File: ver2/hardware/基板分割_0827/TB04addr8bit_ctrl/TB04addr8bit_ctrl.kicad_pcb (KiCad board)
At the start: 2 copper layers, 210 x 170 mm, 101 parts, among them IC401 74HC161N, IC402 74HC161N, IC601 74HC161N, J1 Conn_02x20_Odd_Even, J1602 Screw_Terminal_01x02, J2 Conn_02x20_Odd_Even, J3 Conn_02x10_Odd_Even, J6 Conn_02x05_Odd_Even, J7 Conn_02x05_Odd_Even, J8 Conn_02x05_Odd_Even, J801 Conn_02x05_Odd_Even, J802 Conn_02x05_Odd_Even, J803 Conn_02x05_Odd_Even, J804 Conn_02x05_Odd_Even, J9 Conn_02x05_Odd_Even, SW601 SW_Coded_SH-7050, U101 74HC157, U1101 6116, U1102 74HC244, U1103 74HC244, U1201 74HC193, U1301 74HC08, U1401 74HC138, U1402 74HC244, U1403 74HC244, U1404 74HC244, U1405 74HC244, U1406 74HC157, U1407 74HC139, U1501 74AHC04, U1503 74HC08, U1504 74HC00, U1505 74HC00, U1506 74HC32, U1509 74HC10, U401 74HC157, U404 74HC157, U601 74HC273, U602 74HC273, U604 28C256, U606 74HC273, U607 74HC238, U701 74HC273, U703 28C256, U705 74HC273, U706 28C256

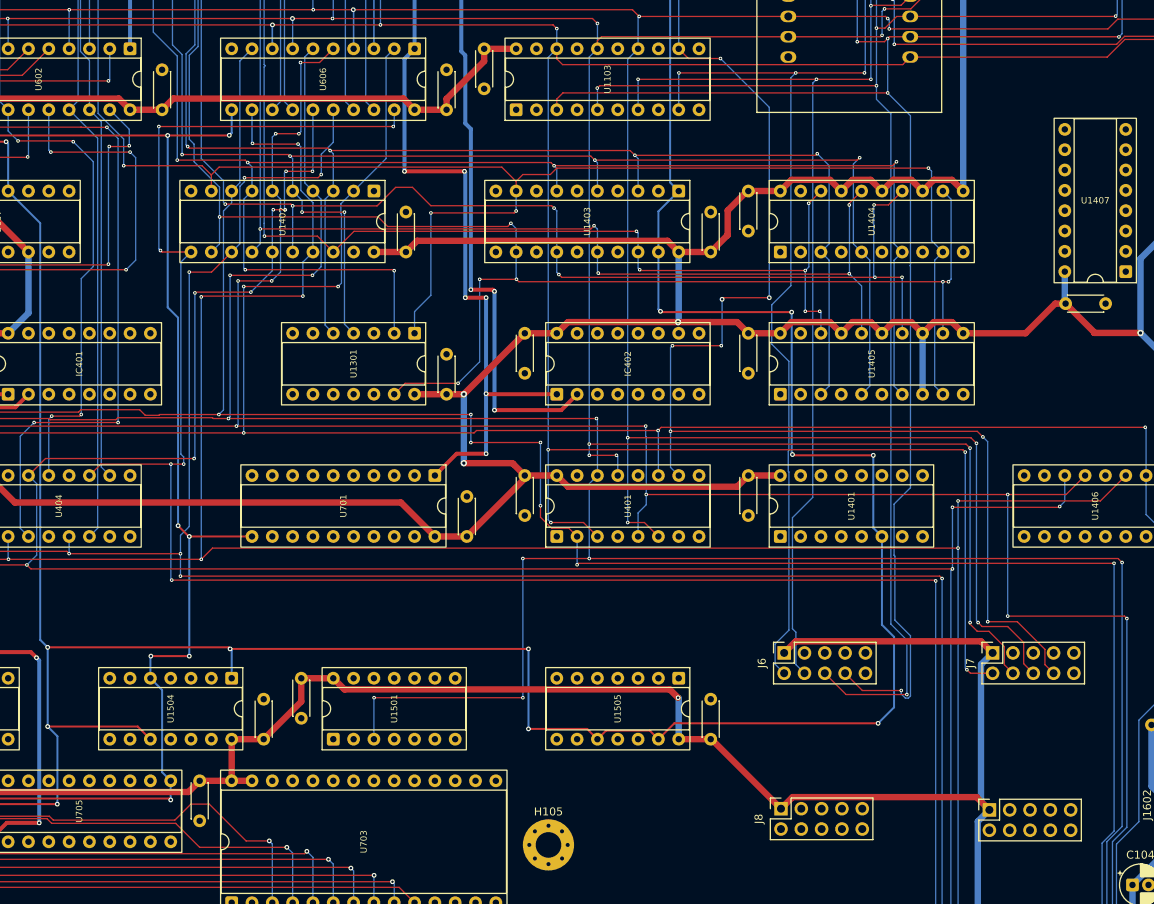
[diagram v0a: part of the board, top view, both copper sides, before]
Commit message: ver2: 制御板の群7(PC_Q0-7)を配線(24接続・DRC 0件)
Co-Authored-By: Claude Opus 5 <noreply@anthropic.com>
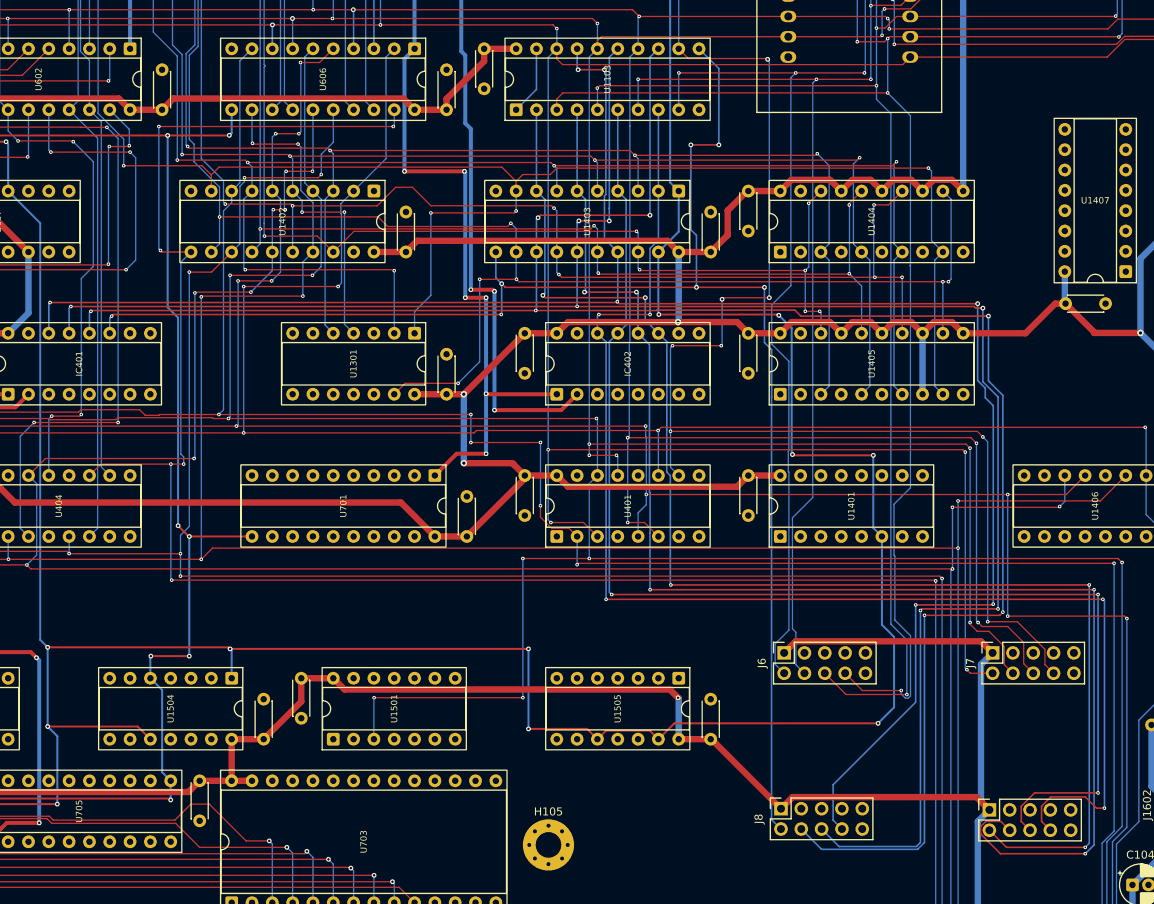
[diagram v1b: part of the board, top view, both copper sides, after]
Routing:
- net PC_Q6: track 0.00 -> 255.4 mm, vias 0 -> 7
- net PC_Q5: track 0.00 -> 244.7 mm, vias 0 -> 7
- net PC_Q4: track 0.00 -> 236.7 mm, vias 0 -> 7
- net PC_Q7: track 0.00 -> 195.5 mm, vias 0 -> 7
- net PC_Q2: track 0.00 -> 176.0 mm, vias 0 -> 5
- net PC_Q3: track 0.00 -> 172.1 mm, vias 0 -> 5
- net PC_Q0: track 0.00 -> 169.2 mm, vias 0 -> 5
- net PC_Q1: track 0.00 -> 161.4 mm, vias 0 -> 3
- net ~{YEN_PC}: track 0.00 -> 8.67 mm
- net MD0: track 418.5 -> 421.9 mm
- net EXE: track 501.4 -> 500.6 mm

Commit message: ver2: 制御板のSP0-2を配線(12接続・DRC 0件)
Co-Authored-By: Claude Opus 5 <noreply@anthropic.com>
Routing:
- net SP0: track 0.00 -> 406.0 mm, vias 0 -> 7
- net SP2: track 0.00 -> 401.7 mm, vias 0 -> 8
- net SP1: track 0.00 -> 388.9 mm, vias 0 -> 6
- net Net-(U1506-Pad3): track 0.00 -> 2.54 mm
- net OPC3: track 282.6 -> 284.6 mm

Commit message: ver2: 制御板のPC0-7を配線(8接続・DRC 0件)
Co-Authored-By: Claude Opus 5 <noreply@anthropic.com>
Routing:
- net PC3: track 0.00 -> 41.1 mm, vias 0 -> 2
- net PC1: track 0.00 -> 34.6 mm, vias 0 -> 4
- net PC6: track 0.00 -> 22.9 mm
- net PC0: track 0.00 -> 22.1 mm, vias 0 -> 2
- net PC4: track 0.00 -> 18.6 mm
- net PC7: track 0.00 -> 11.2 mm
- net PC5: track 0.00 -> 10.2 mm
- net PC2: track 0.00 -> 10.2 mm

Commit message: ver2: 制御板のport0/1・PC_CNT_EN・WR・P2を配線(15接続・DRC 0件)
Co-Authored-By: Claude Opus 5 <noreply@anthropic.com>
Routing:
- net WR: track 0.00 -> 275.5 mm, vias 0 -> 3
- net PC_CNT_EN: track 0.00 -> 156.9 mm, vias 0 -> 5
- net P2: track 0.00 -> 141.5 mm, vias 0 -> 3
- net port0: track 0.00 -> 78.6 mm, vias 0 -> 2
- net port1: track 0.00 -> 71.2 mm, vias 0 -> 2
- net VDD: track 1346.1 -> 1350.0 mm, vias 5 -> 6
- net A3: track 266.3 -> 267.7 mm

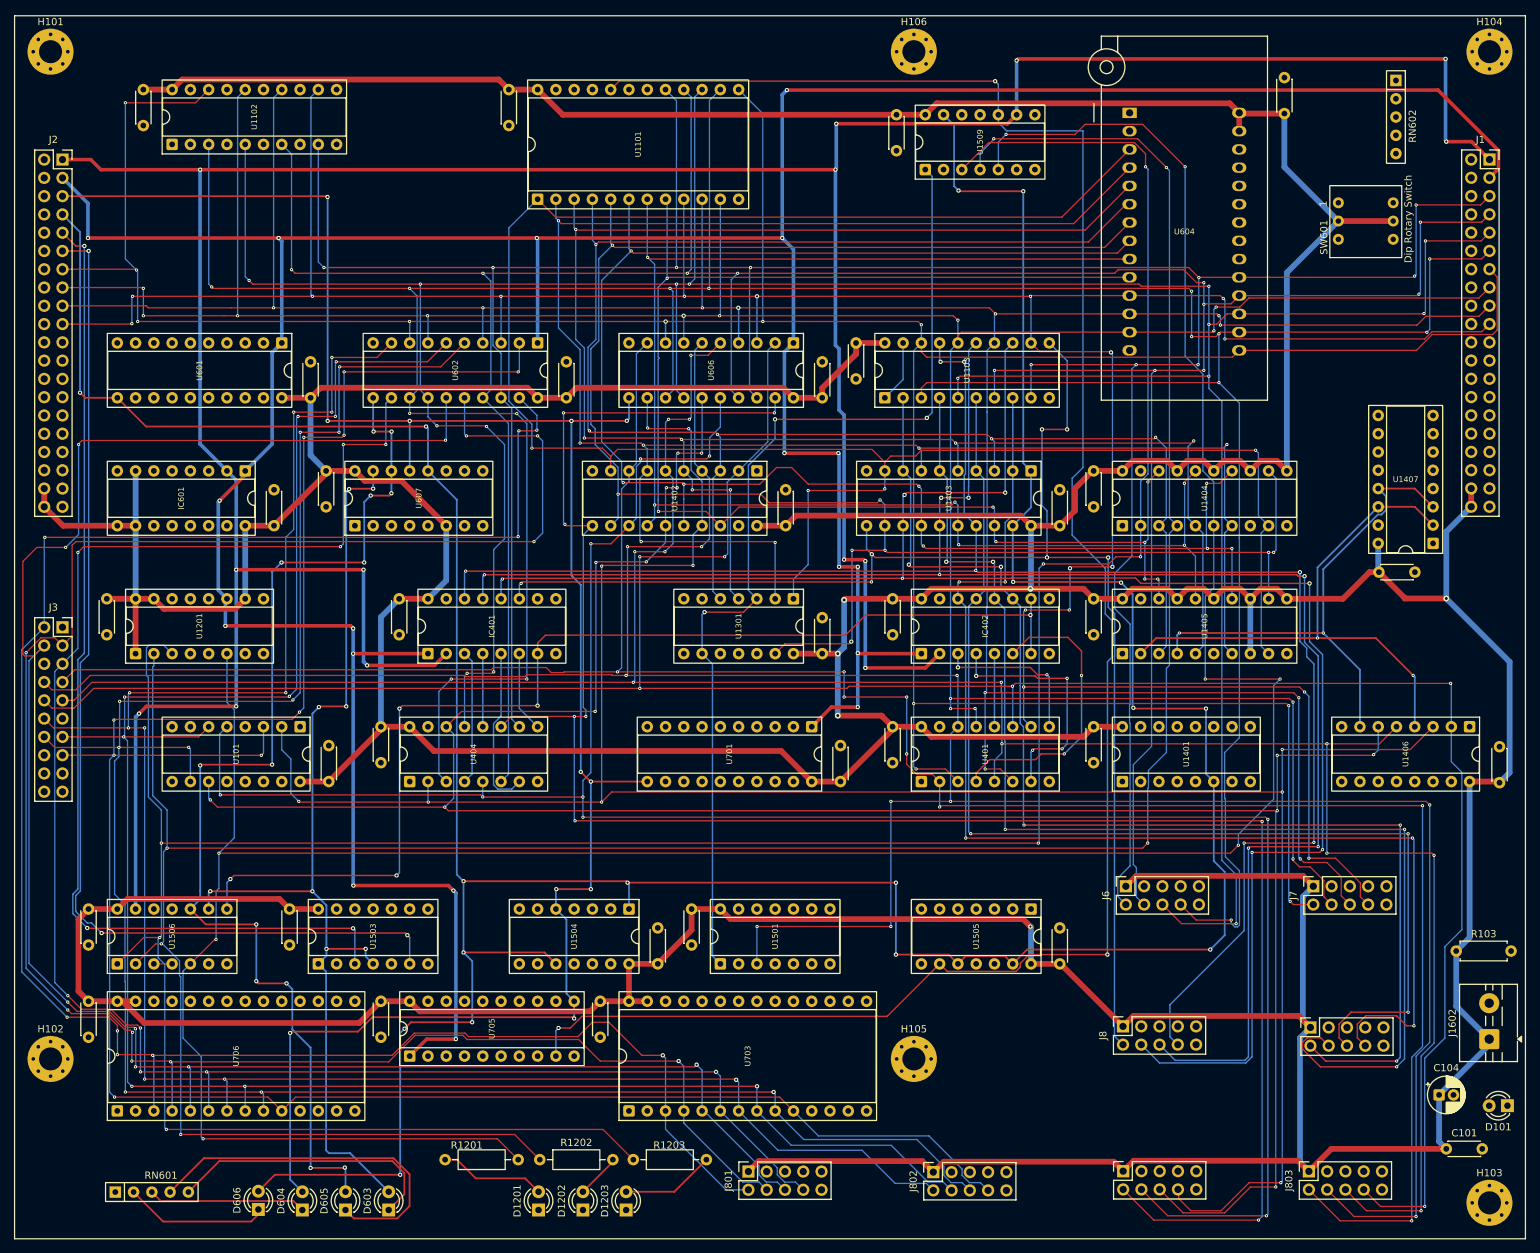
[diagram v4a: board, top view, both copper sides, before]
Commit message: ver2: 制御板の群8を31ネット配線(48接続・DRC 0件)
Co-Authored-By: Claude Opus 5 <noreply@anthropic.com>
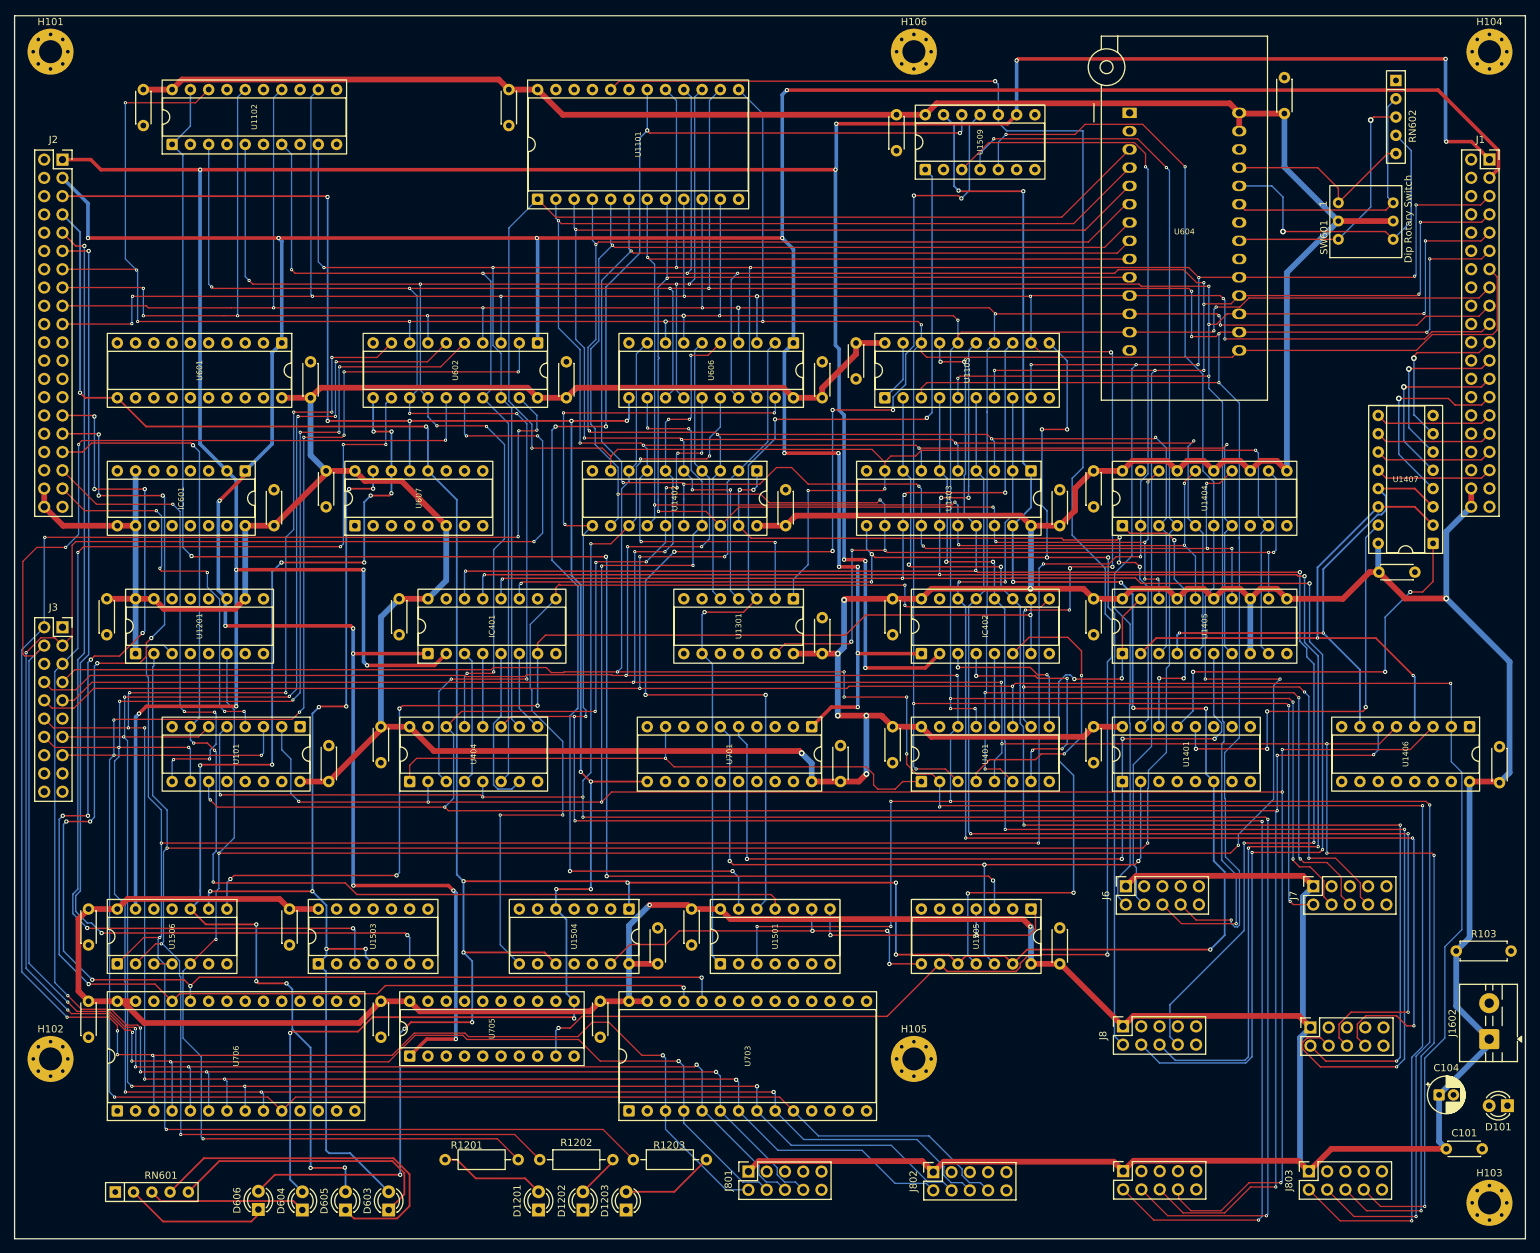
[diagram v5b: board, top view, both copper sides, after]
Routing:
- net ~{YEN_Y}: track 0.00 -> 227.1 mm, vias 0 -> 4
- net ~{CS_RAM}: track 0.00 -> 194.7 mm, vias 0 -> 6
- net zero_prev: track 0.00 -> 193.7 mm, vias 0 -> 10
- net carry_in: track 0.00 -> 187.7 mm, vias 0 -> 9
- net CS_RAM: track 0.00 -> 169.0 mm, vias 0 -> 8
- net sel_a2: track 0.00 -> 163.7 mm, vias 0 -> 4
- net ~{PC_PE}: track 0.00 -> 137.6 mm, vias 0 -> 4
- net SEL_M0: track 0.00 -> 113.2 mm, vias 0 -> 4
- net SEL_M1: track 0.00 -> 102.0 mm, vias 0 -> 3
- net ~{OE_mAddr}: track 0.00 -> 93.6 mm, vias 0 -> 5
- net SEL_PC: track 0.00 -> 81.2 mm, vias 0 -> 1
- net ~{OE_ioAddr}: track 0.00 -> 76.8 mm, vias 0 -> 4
- net sel_a1: track 0.00 -> 66.1 mm, vias 0 -> 5
- net ~{OE_oAddr}: track 0.00 -> 58.3 mm, vias 0 -> 4
- net ~{OE_iAddr}: track 0.00 -> 56.9 mm, vias 0 -> 3
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
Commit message: ver2: 制御板の群8を29接続配線(DRC 0件・残り信号27)
Co-Authored-By: Claude Opus 5 <noreply@anthropic.com>
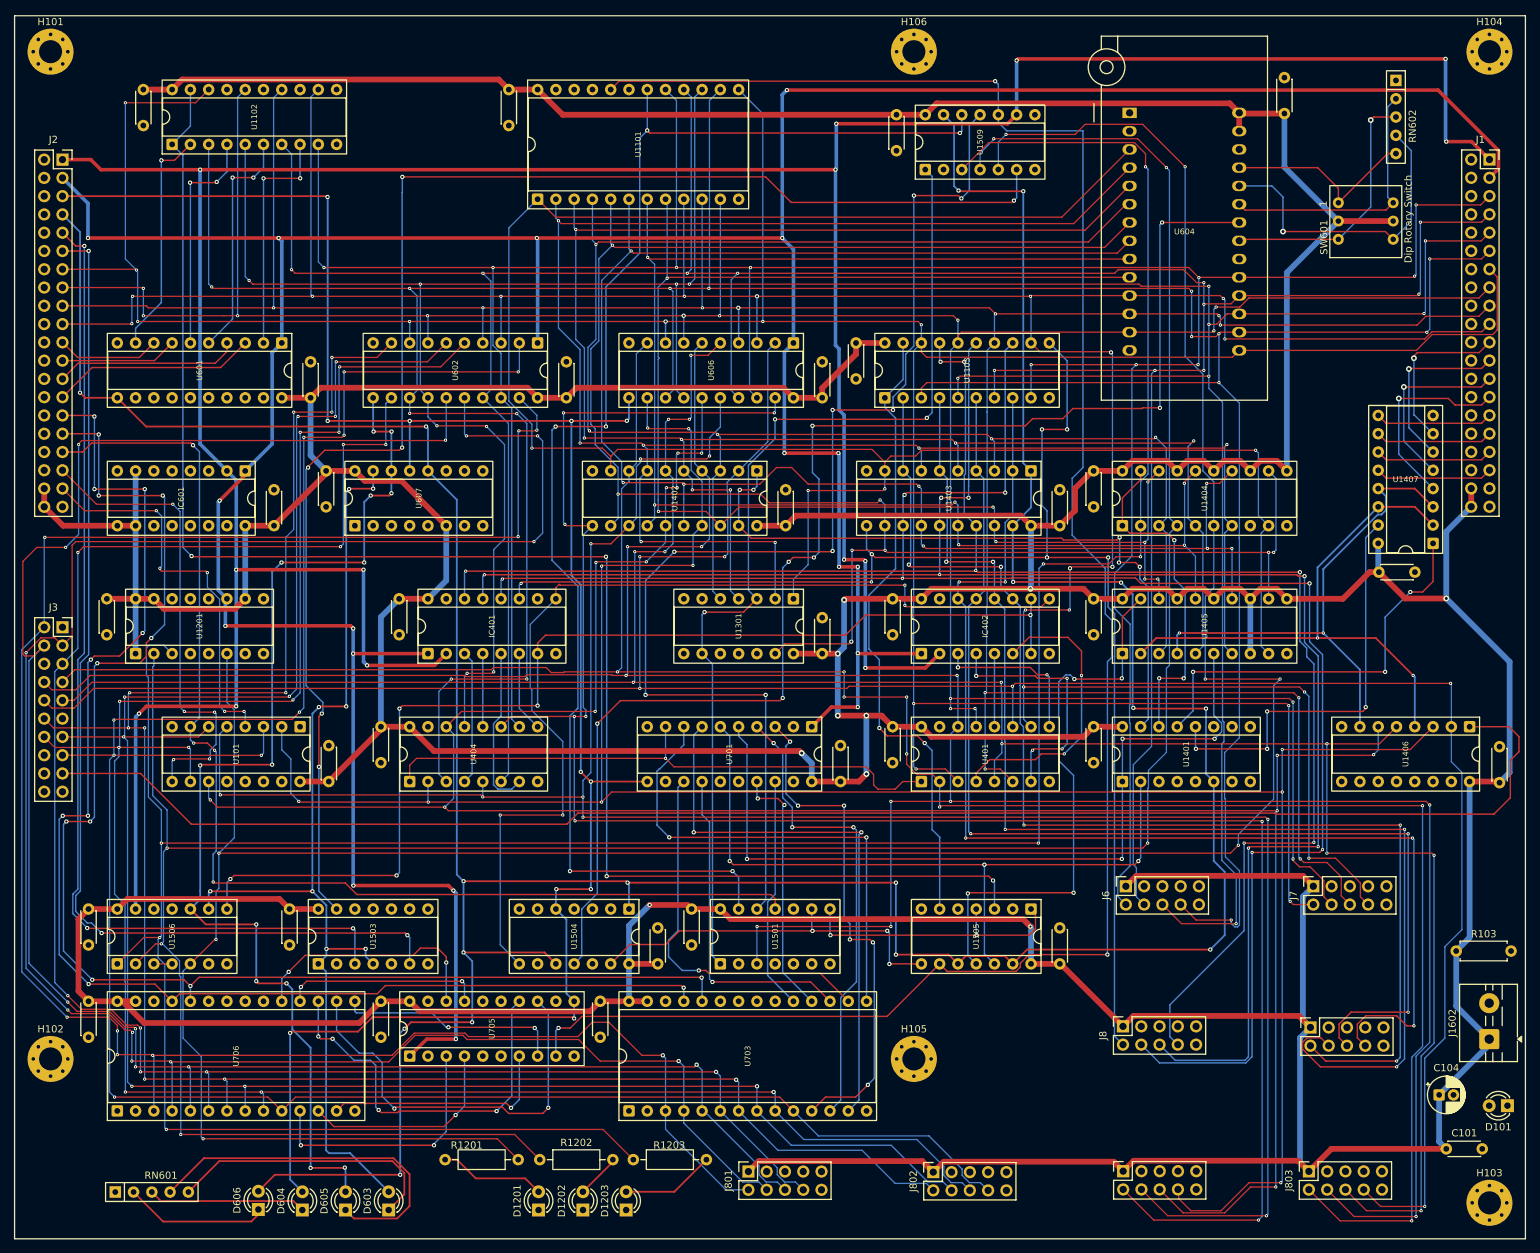
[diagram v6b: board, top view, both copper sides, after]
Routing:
- net SEL_IMM: track 0.00 -> 222.2 mm
- net SP_NE7: track 0.00 -> 206.7 mm, vias 0 -> 6
- net ~{OE_ROM}: track 0.00 -> 189.9 mm, vias 0 -> 7
- net ~{YEN_PC}: track 8.67 -> 88.4 mm, vias 0 -> 2
- net Net-(U701-D2): track 0.00 -> 77.9 mm, vias 0 -> 2
- net Net-(U701-D0): track 0.00 -> 71.0 mm, vias 0 -> 6
- net Net-(U701-D3): track 0.00 -> 67.9 mm, vias 0 -> 2
- net Net-(U701-D1): track 0.00 -> 65.7 mm, vias 0 -> 3
- net Net-(U705-D4): track 0.00 -> 56.9 mm, vias 0 -> 2
- net Net-(U705-D5): track 0.00 -> 54.1 mm, vias 0 -> 4
- net Net-(U701-D4): track 0.00 -> 52.8 mm, vias 0 -> 1
- net Net-(U701-D5): track 0.00 -> 45.9 mm, vias 0 -> 1
- net Net-(U705-D0): track 0.00 -> 36.4 mm, vias 0 -> 2
- net Net-(U701-D6): track 0.00 -> 35.5 mm, vias 0 -> 2
- net Net-(U705-D7): track 0.00 -> 34.4 mm, vias 0 -> 2
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
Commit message: ver2: 制御板の群8を23接続配線(DRC 0件・残り信号4)
Co-Authored-By: Claude Opus 5 <noreply@anthropic.com>
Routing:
- net ~{P5}: track 0.00 -> 133.5 mm, vias 0 -> 1
- net ~{Enb_RS01}: track 0.00 -> 121.5 mm, vias 0 -> 4
- net ~{WE}: track 0.00 -> 120.4 mm, vias 0 -> 5
- net ~{Ena_RS01}: track 0.00 -> 117.1 mm, vias 0 -> 3
- net CD: track 0.00 -> 93.6 mm, vias 0 -> 5
- net P5: track 0.00 -> 86.7 mm, vias 0 -> 6
- net ~{SEL_Y}: track 0.00 -> 76.5 mm, vias 0 -> 3
- net SP_CD: track 0.00 -> 75.6 mm, vias 0 -> 2
- net SP_CU: track 0.00 -> 68.9 mm, vias 0 -> 4
- net PC_LOAD: track 0.00 -> 64.4 mm, vias 0 -> 3
- net RegAddrSrc: track 0.00 -> 64.0 mm, vias 0 -> 6
- net Net-(IC401-CET): track 0.00 -> 63.7 mm, vias 0 -> 3
- net CU_raw: track 0.00 -> 57.4 mm, vias 0 -> 1
- net SEL_Y: track 0.00 -> 45.1 mm, vias 0 -> 5
- net CU: track 0.00 -> 40.8 mm, vias 0 -> 2
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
